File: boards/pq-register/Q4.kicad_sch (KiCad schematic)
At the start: 54 parts, among them Q89 T1-N652, Q90 T1-N652, Q91 T1-N652, Q92 T1-N652, Q93 T1-N652, Q94 T1-N652, Q95 T1-N652, Q96 T1-N652

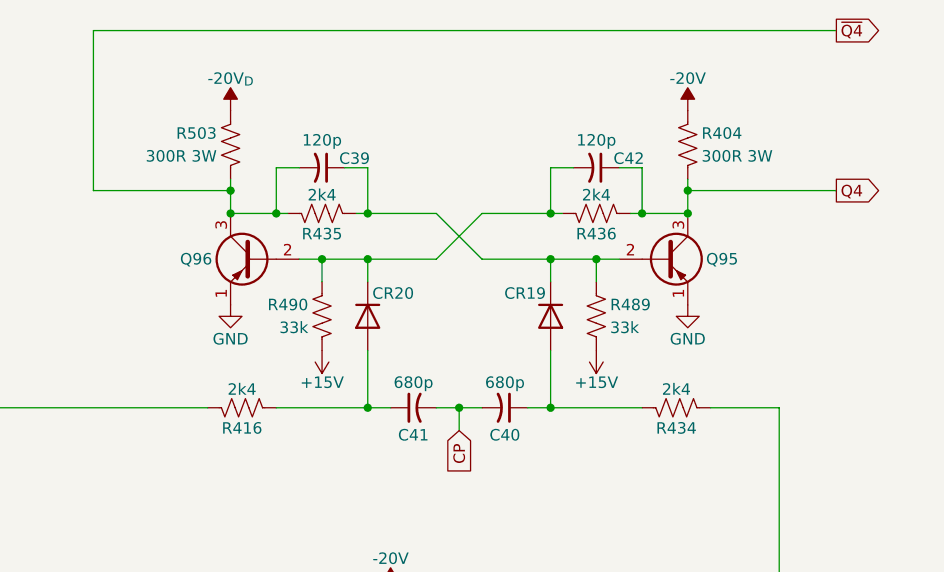
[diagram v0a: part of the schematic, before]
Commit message: Run ERC and clean up P & Q Register board.
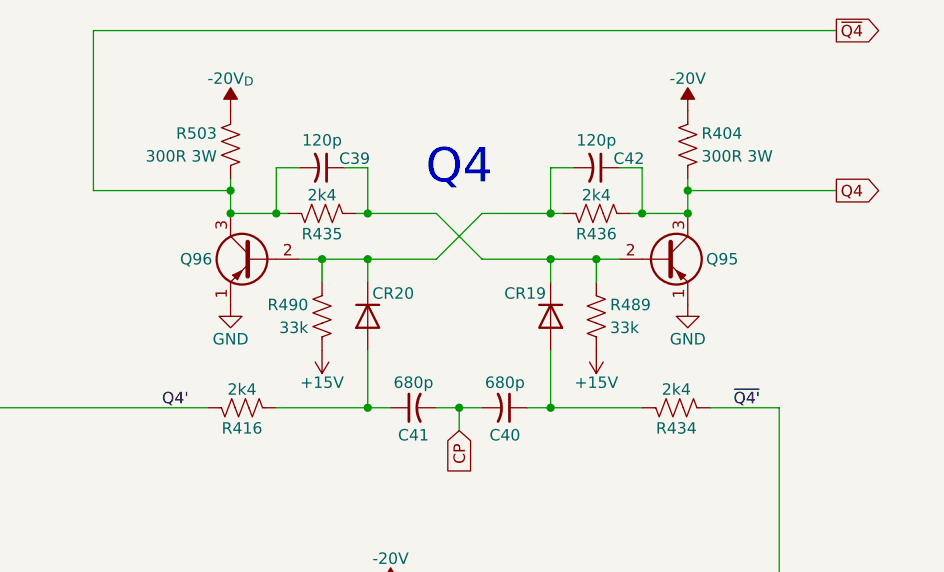
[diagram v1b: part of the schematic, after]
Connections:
- net Q4': now reaches Q90.3 (C), R416.1, R480.2
- net ~{Q4'}: now reaches Q94.3 (C), R434.2, R488.2
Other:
- note added: "Q4"
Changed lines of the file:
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@@
 		(title "LGP-21 P & Q Register Board")
 	)
+	(text "Q4"
+		(exclude_from_sim no)
+		(at 179.07 40.64 0)
+		(effects
+			(font
+				(size 3.81 3.81)
+			)
+		)
+	)
 	(junction
 		(at 101.6 140.97)
@@
 		)
 	)
+	(label "~{Q4'}"
+		(at 209.55 67.31 0)
+		(effects
+			(font
+				(size 1.27 1.27)
+			)
+			(justify left bottom)
+		)
+	)
+	(label "Q4'"
+		(at 146.05 67.31 0)
+		(effects
+			(font
+				(size 1.27 1.27)
+			)
+			(justify left bottom)
+		)
+	)

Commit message: Add copyright information.
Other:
- company: (none) -> © 1962 General Precision; redrawn by Sam Hanes
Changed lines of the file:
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@@
 	(title_block
 		(title "LGP-21 P & Q Register Board")
+		(date "2026-06-15")
+		(rev "ESD 1060")
+		(company "© 1962 General Precision; redrawn by Sam Hanes")
+		(comment 1 "https://github.com/Elemecca/lgp21-docs")
 	)
 	(text "Q4"
